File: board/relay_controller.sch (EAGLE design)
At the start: 41 parts, among them IC1 STM32F103C8T, IC3 AT24C, J1 22-27-2021-02, X1 RJ45-8L21-S, X2 RJ45-8L21-S

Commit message: add factory reset button
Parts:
- added R6: 10k, rcl:R-EU_R0603
- added S2: (no value), SparkFun-Switches:MOMENTARY-SWITCH-SPST-2-SMD-4.6X2.8MM
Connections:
- new net N$7: IC1MCU.PC14, R6.1, S2.3, S2.4
- net +3V3: now also R6.2
- net GND: now also S2.1, S2.2
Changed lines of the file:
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@@
 <part name="F1" library="SparkFun-Fuses" deviceset="PPTC" device="_HALF-AMP" value="6V/0.5A"/>
 <part name="F2" library="SparkFun-Fuses" deviceset="PPTC" device="_HALF-AMP" value="12V/50mA"/>
+<part name="R6" library="rcl" deviceset="R-EU_" device="R0603" value="10k"/>
+<part name="+3V4" library="supply1" deviceset="+3V3" device=""/>
+<part name="GND8" library="supply1" deviceset="GND" device=""/>
+<part name="S2" library="SparkFun-Switches" deviceset="MOMENTARY-SWITCH-SPST-2" device="-SMD-4.6X2.8MM"/>
 </parts>
 <sheets>
@@
 <instance part="F1" gate="G$1" x="109.22" y="0"/>
 <instance part="F2" gate="G$1" x="83.82" y="25.4"/>
+<instance part="R6" gate="G$1" x="-60.96" y="86.36" rot="R180"/>
+<instance part="+3V4" gate="G$1" x="-71.12" y="86.36" rot="R90"/>
+<instance part="GND8" gate="1" x="-50.8" y="111.76" rot="R180"/>
+<instance part="S2" gate="G$1" x="-48.26" y="101.6" rot="R270"/>
 </instances>
 <busses>
@@
 <wire x1="99.06" y1="-7.62" x2="104.14" y2="-7.62" width="0.1524" layer="91"/>
 </segment>
+<segment>
+<pinref part="GND8" gate="1" pin="GND"/>
+<pinref part="S2" gate="G$1" pin="1"/>
+<pinref part="S2" gate="G$1" pin="2"/>
+<wire x1="-48.26" y1="106.68" x2="-50.8" y2="106.68" width="0.1524" layer="91"/>
+<junction x="-50.8" y="106.68"/>
+<wire x1="-50.8" y1="109.22" x2="-50.8" y2="106.68" width="0.1524" layer="91"/>
+</segment>
 </net>
 <net name="+3V3" class="0">
@@
 <wire x1="116.84" y1="0" x2="121.92" y2="0" width="0.1524" layer="91"/>
 </segment>
+<segment>
+<pinref part="R6" gate="G$1" pin="2"/>
+<pinref part="+3V4" gate="G$1" pin="+3V3"/>
+<wire x1="-68.58" y1="86.36" x2="-66.04" y2="86.36" width="0.1524" layer="91"/>
+</segment>
 </net>
 <net name="RELAY_16" class="0">
@@
 </segment>
 </net>
+<net name="N$7" class="0">
+<segment>
+<pinref part="S2" gate="G$1" pin="3"/>
+<pinref part="S2" gate="G$1" pin="4"/>
+<wire x1="-48.26" y1="96.52" x2="-50.8" y2="96.52" width="0.1524" layer="91"/>
+<pinref part="IC1" gate="MCU" pin="PC14"/>
+<wire x1="-63.5" y1="86.36" x2="-55.88" y2="86.36" width="0.1524" layer="91"/>
+<pinref part="R6" gate="G$1" pin="1"/>
+<wire x1="-55.88" y1="86.36" x2="-50.8" y2="86.36" width="0.1524" layer="91"/>
+<wire x1="-50.8" y1="86.36" x2="-45.72" y2="86.36" width="0.1524" layer="91"/>
+<wire x1="-50.8" y1="96.52" x2="-50.8" y2="86.36" width="0.1524" layer="91"/>
+<junction x="-50.8" y="96.52"/>
+<junction x="-50.8" y="86.36"/>
+</segment>
+</net>

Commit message: add tamper, uart
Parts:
- removed J1: 22-27-2021-02, con-molex:22-27-2021-02
- added C11: 10nF, eagle-ltspice:CC0402
- added D18: BAS70-04, diode:BAS70-04
- added POWER, TAMPER: (no value), SparkFun-Connectors:CONN_023.5MM
- added R59: 10k, rcl:R-EU_R0402
- added R60, R61: 100, rcl:R-EU_R0402
- added R62: 1k, rcl:R-EU_R0402
- added UART: (no value), SparkFun-Connectors:CONN_02
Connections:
- new net ASDASD: D18.C1A2, R61.1, R62.2
- new net N$10: R60.1, TAMPER.2
- new net N$5: C11.2, R59.1, R62.1, TAMPER.1
- new net TAMPER: IC1MCU.PB5, R61.2
- new net UART_RX: IC1MCU.PA10, UART.1
- new net UART_TX: IC1MCU.PA9, UART.2
- net +3V3: now also D18.C2, R60.2
- net GND: now also C11.1, D18.A1, POWER.2, R59.2; no longer J1-2.S
- net N$4: now also POWER.1; no longer J1-1.S
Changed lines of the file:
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@@
 <part name="GND5" library="supply1" deviceset="GND" device=""/>
 <part name="+3V3" library="supply1" deviceset="+3V3" device=""/>
-<part name="J1" library="con-molex" deviceset="22-?-02" device="27-2021"/>
 <part name="P+2" library="supply1" deviceset="+12V" device=""/>
 <part name="GND1" library="supply1" deviceset="GND" device=""/>
@@
 <part name="GND8" library="supply1" deviceset="GND" device=""/>
 <part name="S2" library="SparkFun-Switches" deviceset="MOMENTARY-SWITCH-SPST-2" device="-SMD-4.6X2.8MM"/>
+<part name="UART" library="SparkFun-Connectors" deviceset="CONN_02" device=""/>
+<part name="TAMPER" library="SparkFun-Connectors" deviceset="CONN_02" device="3.5MM"/>
+<part name="+3V30" library="supply1" deviceset="+3V3" device=""/>
+<part name="GND85" library="supply1" deviceset="GND" device=""/>
+<part name="R59" library="rcl" deviceset="R-EU_" device="R0402" value="10k"/>
+<part name="GND86" library="supply1" deviceset="GND" device=""/>
+<part name="C11" library="eagle-ltspice" deviceset="C" device="C0402" value="10nF"/>
+<part name="D18" library="diode" deviceset="BAS70-04" device=""/>
+<part name="+3V31" library="supply1" deviceset="+3V3" device=""/>
+<part name="GND87" library="supply1" deviceset="GND" device=""/>
+<part name="R60" library="rcl" deviceset="R-EU_" device="R0402" value="100"/>
+<part name="R61" library="rcl" deviceset="R-EU_" device="R0402" value="100"/>
+<part name="R62" library="rcl" deviceset="R-EU_" device="R0402" value="1k"/>
+<part name="POWER" library="SparkFun-Connectors" deviceset="CONN_02" device="3.5MM"/>
 </parts>
 <sheets>
@@
 <instance part="GND5" gate="1" x="48.26" y="27.94" rot="R90"/>
 <instance part="+3V3" gate="G$1" x="22.86" y="40.64" rot="R90"/>
-<instance part="J1" gate="-1" x="96.52" y="25.4"/>
-<instance part="J1" gate="-2" x="96.52" y="20.32"/>
 <instance part="P+2" gate="1" x="73.66" y="25.4" rot="R90"/>
-<instance part="GND1" gate="1" x="88.9" y="20.32" rot="R270"/>
+<instance part="GND1" gate="1" x="93.98" y="17.78"/>
 <instance part="U$1" gate="G$1" x="88.9" y="-12.7" rot="R180"/>
 <instance part="P+1" gate="1" x="114.3" y="-15.24" rot="R270"/>
@@
 <instance part="GND8" gate="1" x="-50.8" y="111.76" rot="R180"/>
 <instance part="S2" gate="G$1" x="-48.26" y="101.6" rot="R270"/>
+<instance part="UART" gate="G$1" x="-160.02" y="109.22"/>
+<instance part="TAMPER" gate="G$1" x="-172.72" y="66.04" rot="R180"/>
+<instance part="+3V30" gate="G$1" x="-205.74" y="63.5" rot="R90"/>
+<instance part="GND85" gate="1" x="-182.88" y="81.28" rot="R180"/>
+<instance part="R59" gate="G$1" x="-182.88" y="71.12" rot="R90"/>
+<instance part="GND86" gate="1" x="-198.12" y="81.28" rot="R180"/>
+<instance part="C11" gate="G$1" x="-198.12" y="73.66"/>
+<instance part="D18" gate="G$1" x="-218.44" y="81.28" rot="R180"/>
+<instance part="+3V31" gate="G$1" x="-231.14" y="81.28" rot="R90"/>
+<instance part="GND87" gate="1" x="-208.28" y="81.28" rot="R90"/>
+<instance part="R60" gate="G$1" x="-187.96" y="63.5" rot="R180"/>
+<instance part="R61" gate="G$1" x="-246.38" y="66.04" rot="R180"/>
+<instance part="R62" gate="G$1" x="-208.28" y="66.04" rot="R180"/>
+<instance part="POWER" gate="G$1" x="101.6" y="25.4" rot="R180"/>
 </instances>
 <busses>
@@
 </segment>
 <segment>
-<pinref part="J1" gate="-2" pin="S"/>
 <pinref part="GND1" gate="1" pin="GND"/>
-<wire x1="91.44" y1="20.32" x2="93.98" y2="20.32" width="0.1524" layer="91"/>
+<wire x1="93.98" y1="20.32" x2="93.98" y2="22.86" width="0.1524" layer="91"/>
+<pinref part="POWER" gate="G$1" pin="2"/>
 </segment>
 <segment>
@@
 <junction x="-50.8" y="106.68"/>
 <wire x1="-50.8" y1="109.22" x2="-50.8" y2="106.68" width="0.1524" layer="91"/>
+</segment>
+<segment>
+<pinref part="GND85" gate="1" pin="GND"/>
+<pinref part="R59" gate="G$1" pin="2"/>
+<wire x1="-182.88" y1="78.74" x2="-182.88" y2="76.2" width="0.1524" layer="91"/>
+</segment>
+<segment>
+<pinref part="GND86" gate="1" pin="GND"/>
+<pinref part="C11" gate="G$1" pin="1"/>
+<wire x1="-198.12" y1="78.74" x2="-198.12" y2="76.2" width="0.1524" layer="91"/>
+</segment>
+<segment>
+<pinref part="D18" gate="G$1" pin="A1"/>
+<pinref part="GND87" gate="1" pin="GND"/>
+<wire x1="-213.36" y1="81.28" x2="-210.82" y2="81.28" width="0.1524" layer="91"/>
 </segment>
 </net>
@@
 <wire x1="-68.58" y1="86.36" x2="-66.04" y2="86.36" width="0.1524" layer="91"/>
 </segment>
+<segment>
+<pinref part="+3V31" gate="G$1" pin="+3V3"/>
+<pinref part="D18" gate="G$1" pin="C2"/>
+<wire x1="-228.6" y1="81.28" x2="-223.52" y2="81.28" width="0.1524" layer="91"/>
+</segment>
+<segment>
+<pinref part="R60" gate="G$1" pin="2"/>
+<pinref part="+3V30" gate="G$1" pin="+3V3"/>
+<wire x1="-193.04" y1="63.5" x2="-203.2" y2="63.5" width="0.1524" layer="91"/>
+</segment>
 </net>
 <net name="RELAY_16" class="0">
@@
 <net name="N$4" class="0">
 <segment>
-<pinref part="J1" gate="-1" pin="S"/>
 <pinref part="F2" gate="G$1" pin="2"/>
 <wire x1="91.44" y1="25.4" x2="93.98" y2="25.4" width="0.1524" layer="91"/>
+<pinref part="POWER" gate="G$1" pin="1"/>
 </segment>
 </net>
@@
 </segment>
 </net>
+<net name="UART_RX" class="0">
+<segment>
+<pinref part="UART" gate="G$1" pin="1"/>
+<wire x1="-152.4" y1="109.22" x2="-137.16" y2="109.22" width="0.1524" layer="91"/>
+<label x="-137.16" y="109.22" size="1.778" layer="95" xref="yes"/>
+</segment>
+<segment>
+<pinref part="IC1" gate="MCU" pin="PA10"/>
+<wire x1="0" y1="66.04" x2="7.62" y2="66.04" width="0.1524" layer="91"/>
+<label x="7.62" y="66.04" size="1.778" layer="95" xref="yes"/>
+</segment>
+</net>
+<net name="UART_TX" class="0">
+<segment>
+<pinref part="UART" gate="G$1" pin="2"/>
+<wire x1="-152.4" y1="111.76" x2="-142.24" y2="111.76" width="0.1524" layer="91"/>
+<label x="-142.24" y="111.76" size="1.778" layer="95" xref="yes"/>
+</segment>
+<segment>
+<pinref part="IC1" gate="MCU" pin="PA9"/>
+<wire x1="0" y1="63.5" x2="15.24" y2="63.5" width="0.1524" layer="91"/>
+<label x="15.24" y="63.5" size="1.778" layer="95" xref="yes"/>
+</segment>
+</net>
+<net name="ASDASD" class="0">
+<segment>
+<pinref part="D18" gate="G$1" pin="C1A2"/>
+<wire x1="-218.44" y1="78.74" x2="-218.44" y2="66.04" width="0.1524" layer="91"/>
+<wire x1="-218.44" y1="66.04" x2="-241.3" y2="66.04" width="0.1524" layer="91"/>
+<pinref part="R61" gate="G$1" pin="1"/>
+<pinref part="R62" gate="G$1" pin="2"/>
+<wire x1="-213.36" y1="66.04" x2="-218.44" y2="66.04" width="0.1524" layer="91"/>
+<junction x="-218.44" y="66.04"/>
+</segment>
+</net>
+<net name="N$10" class="0">
+<segment>
+<pinref part="R60" gate="G$1" pin="1"/>
+<pinref part="TAMPER" gate="G$1" pin="2"/>
+<wire x1="-182.88" y1="63.5" x2="-180.34" y2="63.5" width="0.1524" layer="91"/>
+</segment>
+</net>
+<net name="N$5" class="0">
+<segment>
+<pinref part="C11" gate="G$1" pin="2"/>
+<wire x1="-198.12" y1="68.58" x2="-198.12" y2="66.04" width="0.1524" layer="91"/>
+<pinref part="R59" gate="G$1" pin="1"/>
+<wire x1="-182.88" y1="66.04" x2="-198.12" y2="66.04" width="0.1524" layer="91"/>
+<junction x="-182.88" y="66.04"/>
+<pinref part="TAMPER" gate="G$1" pin="1"/>
+<wire x1="-180.34" y1="66.04" x2="-182.88" y2="66.04" width="0.1524" layer="91"/>
+<pinref part="R62" gate="G$1" pin="1"/>
+<wire x1="-203.2" y1="66.04" x2="-198.12" y2="66.04" width="0.1524" layer="91"/>
+<junction x="-198.12" y="66.04"/>
+</segment>
+</net>
+<net name="TAMPER" class="0">
+<segment>
+<pinref part="R61" gate="G$1" pin="2"/>
+<wire x1="-251.46" y1="66.04" x2="-261.62" y2="66.04" width="0.1524" layer="91"/>
+<label x="-261.62" y="66.04" size="1.778" layer="95" rot="R180" xref="yes"/>
+</segment>
+<segment>
+<pinref part="IC1" gate="MCU" pin="PB5"/>
+<wire x1="0" y1="96.52" x2="17.78" y2="96.52" width="0.1524" layer="91"/>
+<label x="17.78" y="96.52" size="1.778" layer="95" xref="yes"/>
+</segment>
+</net>

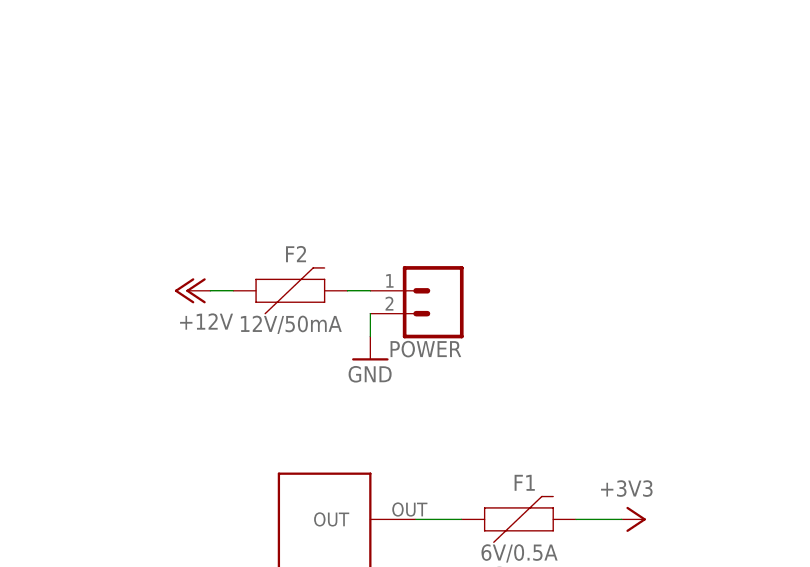
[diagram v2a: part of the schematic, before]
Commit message: add 3.3v output for relay board
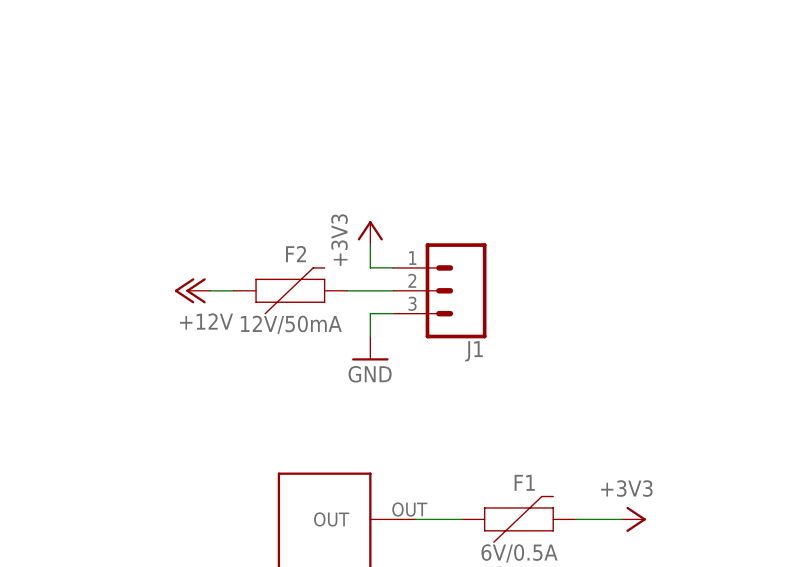
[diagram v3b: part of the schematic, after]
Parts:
- removed POWER: (no value), SparkFun-Connectors:CONN_023.5MM
- added J1: (no value), SparkFun-Connectors:CONN_03SCREW
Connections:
- net +3V3: now also J1.1
- net GND: now also J1.3; no longer POWER.2
- net N$4: now also J1.2; no longer POWER.1
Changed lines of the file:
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@@
 <part name="R61" library="rcl" deviceset="R-EU_" device="R0402" value="100"/>
 <part name="R62" library="rcl" deviceset="R-EU_" device="R0402" value="1k"/>
-<part name="POWER" library="SparkFun-Connectors" deviceset="CONN_02" device="3.5MM"/>
+<part name="+3V11" library="supply1" deviceset="+3V3" device=""/>
+<part name="J1" library="SparkFun-Connectors" deviceset="CONN_03" device="SCREW"/>
 </parts>
 <sheets>
@@
 <instance part="R61" gate="G$1" x="-246.38" y="66.04" rot="R180"/>
 <instance part="R62" gate="G$1" x="-208.28" y="66.04" rot="R180"/>
-<instance part="POWER" gate="G$1" x="101.6" y="25.4" rot="R180"/>
+<instance part="+3V11" gate="G$1" x="93.98" y="33.02"/>
+<instance part="J1" gate="J$1" x="104.14" y="25.4" rot="R180"/>
 </instances>
 <busses>
@@
 </segment>
 <segment>
-<pinref part="GND1" gate="1" pin="GND"/>
-<wire x1="93.98" y1="20.32" x2="93.98" y2="22.86" width="0.1524" layer="91"/>
-<pinref part="POWER" gate="G$1" pin="2"/>
-</segment>
-<segment>
 <pinref part="U$1" gate="G$1" pin="GND"/>
 <pinref part="GND3" gate="1" pin="GND"/>
@@
 <pinref part="GND87" gate="1" pin="GND"/>
 <wire x1="-213.36" y1="81.28" x2="-210.82" y2="81.28" width="0.1524" layer="91"/>
+</segment>
+<segment>
+<pinref part="GND1" gate="1" pin="GND"/>
+<wire x1="96.52" y1="22.86" x2="93.98" y2="22.86" width="0.1524" layer="91"/>
+<wire x1="93.98" y1="22.86" x2="93.98" y2="20.32" width="0.1524" layer="91"/>
+<pinref part="J1" gate="J$1" pin="3"/>
 </segment>
 </net>
@@
 <wire x1="-193.04" y1="63.5" x2="-203.2" y2="63.5" width="0.1524" layer="91"/>
 </segment>
+<segment>
+<pinref part="+3V11" gate="G$1" pin="+3V3"/>
+<wire x1="96.52" y1="27.94" x2="93.98" y2="27.94" width="0.1524" layer="91"/>
+<wire x1="93.98" y1="27.94" x2="93.98" y2="30.48" width="0.1524" layer="91"/>
+<pinref part="J1" gate="J$1" pin="1"/>
+</segment>
 </net>
 <net name="RELAY_16" class="0">
@@
 </segment>
 </net>
-<net name="N$4" class="0">
-<segment>
-<pinref part="F2" gate="G$1" pin="2"/>
-<wire x1="91.44" y1="25.4" x2="93.98" y2="25.4" width="0.1524" layer="91"/>
-<pinref part="POWER" gate="G$1" pin="1"/>
-</segment>
-</net>
 <net name="N$7" class="0">
 <segment>
@@
 </segment>
 </net>
+<net name="N$4" class="0">
+<segment>
+<pinref part="F2" gate="G$1" pin="2"/>
+<wire x1="96.52" y1="25.4" x2="91.44" y2="25.4" width="0.1524" layer="91"/>
+<pinref part="J1" gate="J$1" pin="2"/>
+</segment>
+</net>
